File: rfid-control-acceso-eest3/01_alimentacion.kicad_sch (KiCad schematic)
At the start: 16 parts, among them J1 BOARD_12VDC_2.5A, J2 BUCK?

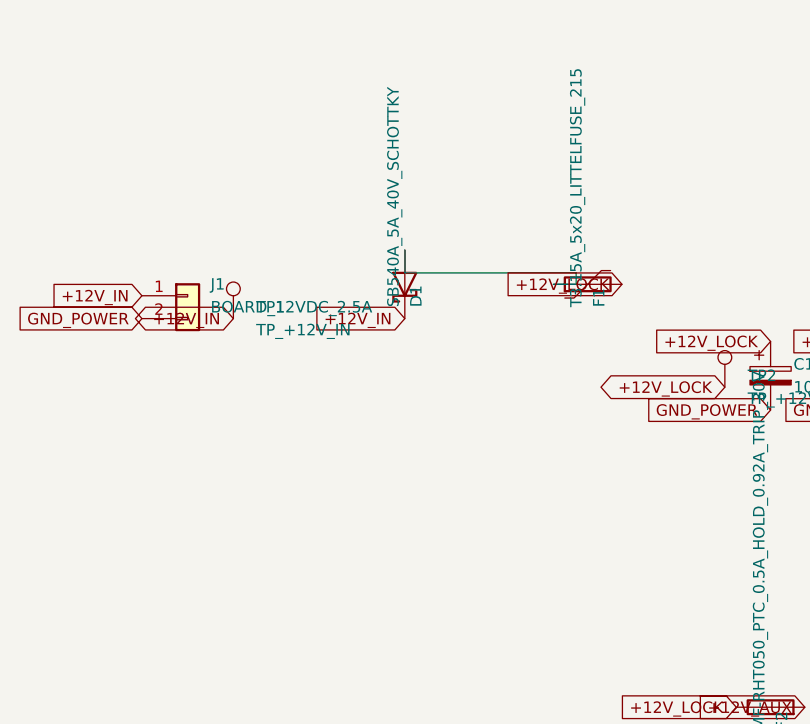
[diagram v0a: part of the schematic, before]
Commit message: Corrige tres diodos invertidos, netclasses y recalcula el floorplan
Errores electricos, verificados regenerando el netlist con kicad-cli:

- D1 tenia el catodo en +12V_IN y el anodo hacia F1, o sea bloqueaba la
  polaridad correcta. Montado asi la placa no encendia.
- D2 y D3 tenian el anodo a GND y el catodo hacia R3/R4. Como un GPIO nunca
  baja de 0 V, los LEDs no podian encender.
- La red entre D1 y F1 no coincidia con ningun patron de netclass y heredaba
  Default: 0,2 mm de pista para ~2,2 A. Pasa a LOCK_POWER (2,0 mm), igual que
  +12V_IN, que estaba en POWER_12V_AUX (0,8 mm).
- Al girar los LEDs, KiCad renombro las redes autogeneradas. Las netclasses
  apuntaban a los nombres viejos; se re-apuntaron.

Footprints: se eliminan los ocho PLACEHOLDER_NO_FABRICAR. Todos tenian
equivalente real ya instalado en KiCad 10. C9 pasa a MLCC 1206: tenia simbolo
no polarizado con footprint de electrolitico. El unico footprint local que
queda es el del ESP32-S3, con la hilera par duplicada en 22,86 y 25,40 mm
porque no se midio el modulo fisico. El paso doble cubre la separacion, no el
orden de pines: hay que verificar 3V3, EN, 5V y GND por continuidad antes de
soldar.

Floorplan: la posicion real de los pines de J13 determina el orden de los
bloques, y estaban casi invertidos. Lazo de potencia J1-J9 de 86 a 38 mm,
estrella de masa NT1-J1 de 60 a 9 mm, SPI de ~70 a 8,7 mm. Contorno de 120x80
a 140x100 mm: la densidad bajaba de 53% a 36% y la caja sigue sin definir.

Sigue sin ruteo, sin vias y sin archivos de fabricacion. Falta ejecutar
Update PCB from Schematic en la GUI: KiCad no expone esa operacion por CLI.

Co-Authored-By: Claude Opus 5 <noreply@anthropic.com>
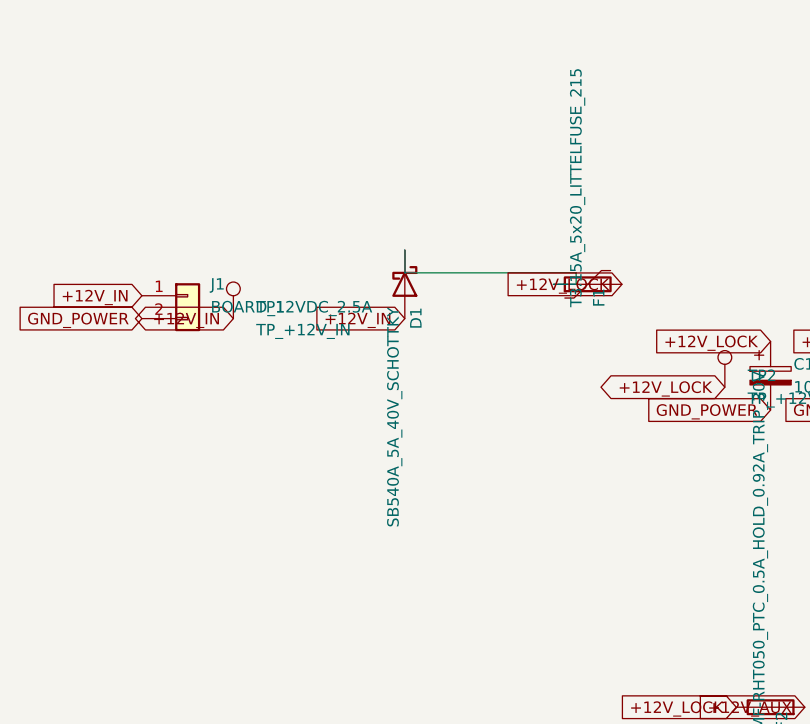
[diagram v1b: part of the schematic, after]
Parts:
- C1: footprint rfid_eest3:CP_Radial_D16_P7.50_PLACEHOLDER_NO_FABRICAR -> Capacitor_THT:CP_Radial_D16.0mm_P7.50mm
- C3: footprint rfid_eest3:CP_Radial_D10_P5.00_PLACEHOLDER_NO_FABRICAR -> Capacitor_THT:CP_Radial_D10.0mm_P5.00mm_P7.50mm
- J1: footprint rfid_eest3:KF301_2P_P5.08_PLACEHOLDER_NO_FABRICAR -> TerminalBlock_RND:TerminalBlock_RND_205-00232_1x02_P5.08mm_Horizontal
- J2: footprint rfid_eest3:KF301_4P_P5.08_PLACEHOLDER_NO_FABRICAR -> TerminalBlock_RND:TerminalBlock_RND_205-00234_1x04_P5.08mm_Horizontal
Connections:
- net +12V_IN: now also D1.2 (A); no longer D1.1 (K)
- net at F1.1: now also D1.1 (K); no longer D1.2 (A)
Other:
- moved on the sheet: D1
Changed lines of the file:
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@@
 			)
 		)
-		(property "Footprint" "rfid_eest3:KF301_4P_P5.08_PLACEHOLDER_NO_FABRICAR"
+		(property "Footprint" "TerminalBlock_RND:TerminalBlock_RND_205-00234_1x04_P5.08mm_Horizontal"
 			(at 144.78 41.91 0)
 			(hide yes)
@@
 	(symbol
 		(lib_id "Device:D_Schottky")
-		(at 54.61 38.1 90)
+		(at 54.61 38.1 270)
 		(unit 1)
 		(body_style 1)
@@
 			)
 		)
-		(property "Footprint" "rfid_eest3:CP_Radial_D10_P5.00_PLACEHOLDER_NO_FABRICAR"
+		(property "Footprint" "Capacitor_THT:CP_Radial_D10.0mm_P5.00mm_P7.50mm"
 			(at 181.3052 44.45 0)
 			(hide yes)
@@
 			)
 		)
-		(property "Footprint" "rfid_eest3:KF301_2P_P5.08_PLACEHOLDER_NO_FABRICAR"
+		(property "Footprint" "TerminalBlock_RND:TerminalBlock_RND_205-00232_1x02_P5.08mm_Horizontal"
 			(at 30.48 39.37 0)
 			(hide yes)
@@
 			)
 		)
-		(property "Footprint" "rfid_eest3:CP_Radial_D16_P7.50_PLACEHOLDER_NO_FABRICAR"
+		(property "Footprint" "Capacitor_THT:CP_Radial_D16.0mm_P7.50mm"
 			(at 96.2152 44.45 0)
 			(hide yes)
